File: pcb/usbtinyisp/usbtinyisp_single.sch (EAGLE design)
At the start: 20 parts, among them IC1 ATTINY2313-20P, IC2 74AHC125N

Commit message: update dimensions and change some packages
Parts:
- D1, D2: value 3.6V -> 3V6; device diode:ZENER-DIODEDO35Z10 -> diode:ZENER-DIODESOD80C
- JP1: device pinhead-ez:PINHD-2X3 -> con-ml:ML6
- R1, R2: value 27 -> 68
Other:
- moved on the sheet: C2, D1, D2, LED1, LED2, R1, R2, R3, R5, R6, X1

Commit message: unsmash
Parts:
- C1: value 0.1uF -> 100n
- C2: value 100uF -> 100u
- R10: value 10K -> 10k
- R3, R4, R5, R6, R7: value 1.5K -> 1k5
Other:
- moved on the sheet: C1, IC2P

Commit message: vergessene Änderungen
wenn man nicht alles gleich commited :-/
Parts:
- removed XTL1: 12.0 MHz, minimidi:CERMOSCILL
- added C3, C4: 22p, rcl:C-EUC1206
- added Q1: 12000, crystal:CRYSTALHC49U-V
- IC2: value 74AHC125N -> 74LVX125D; device 74xx-eu:74HC125N -> 74xx-eu:74HC125D
- R1, R10, R4, R7: device rcl-ez:R-US_0207/10 -> rcl:R-EU_R0805
- R2, R3, R5, R6: device rcl-ez:R-US_0207/5V -> rcl:R-EU_R0805
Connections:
- removed net N$4: IC1.XTAL1(PA0), XTL1.OUT
- removed net N$5: IC1.XTAL2(PA1), XTL1.IN
- new net XTAL1: C4.1, IC1.XTAL1(PA0), Q1.1
- new net XTAL2: C3.1, IC1.XTAL2(PA1), Q1.2
- net GND: now also C3.2, C4.2; no longer XTL1.GND
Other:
- moved on the sheet: C1

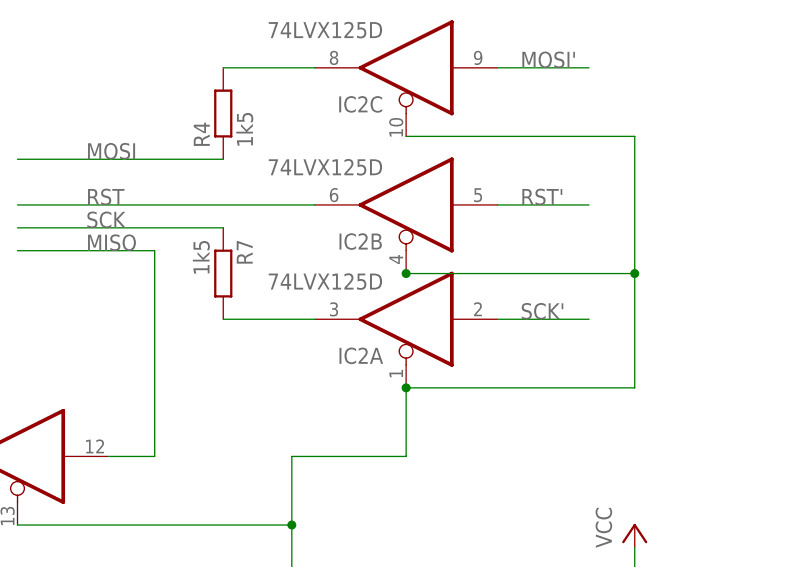
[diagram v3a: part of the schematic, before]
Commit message: swapped some gates and moved all parts around
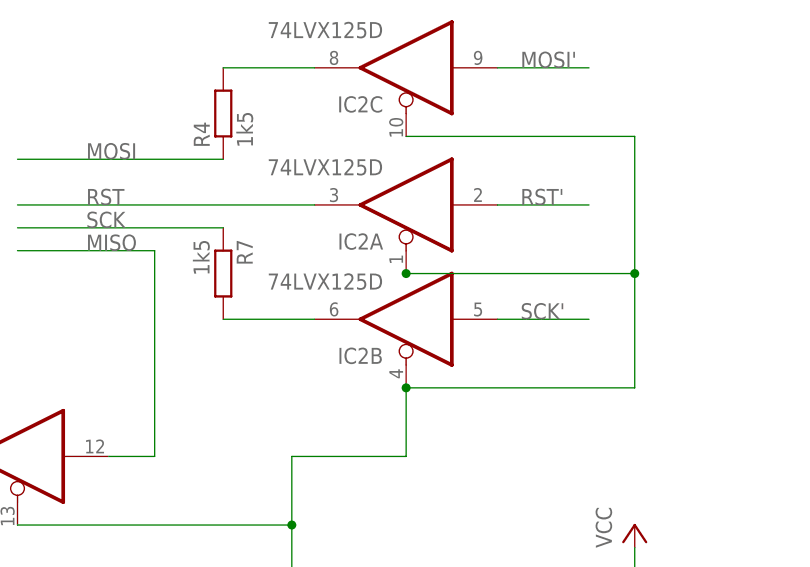
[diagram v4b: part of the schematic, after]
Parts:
- R1, R2: device rcl:R-EU_R0805 -> rcl:R-EU_0207/10
- R7: device rcl:R-EU_R0805 -> rcl:R-EU_0207/12
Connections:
- net N$12: now also IC2B.O; no longer IC2A.O
- net RST: now also IC2A.O; no longer IC2B.O
- net RST': now also IC2A.I; no longer IC2B.I
- net SCK': now also IC2B.I; no longer IC2A.I
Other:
- moved on the sheet: IC2A, IC2B
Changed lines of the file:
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@@
 </classes>
 <parts>
-<part name="R1" library="rcl" deviceset="R-EU_" device="R0805" value="68"/>
-<part name="R2" library="rcl" deviceset="R-EU_" device="R0805" value="68"/>
+<part name="R1" library="rcl" deviceset="R-EU_" device="0207/10" value="68"/>
+<part name="R2" library="rcl" deviceset="R-EU_" device="0207/10" value="68"/>
 <part name="R3" library="rcl" deviceset="R-EU_" device="R0805" value="1k5"/>
 <part name="GND1" library="supply1" deviceset="GND" device=""/>
@@
 <part name="D1" library="diode" deviceset="ZENER-DIODE" device="SOD80C" value="3V6"/>
 <part name="D2" library="diode" deviceset="ZENER-DIODE" device="SOD80C" value="3V6"/>
-<part name="R7" library="rcl" deviceset="R-EU_" device="R0805" value="1k5"/>
+<part name="R7" library="rcl" deviceset="R-EU_" device="0207/12" value="1k5"/>
 <part name="R4" library="rcl" deviceset="R-EU_" device="R0805" value="1k5"/>
 <part name="P+3" library="supply1" deviceset="VCC" device=""/>
@@
 <instance part="JP1" gate="1" x="53.34" y="152.4" rot="MR180"/>
 <instance part="X1" gate="G$1" x="20.32" y="76.2" rot="MR0"/>
-<instance part="IC2" gate="A" x="127" y="142.24" rot="R180"/>
-<instance part="IC2" gate="B" x="127" y="154.94" rot="R180"/>
+<instance part="IC2" gate="B" x="127" y="142.24" rot="R180"/>
+<instance part="IC2" gate="A" x="127" y="154.94" rot="R180"/>
 <instance part="IC2" gate="C" x="127" y="170.18" rot="R180"/>
 <instance part="IC2" gate="D" x="83.82" y="127" rot="R180"/>
@@
 <wire x1="116.84" y1="154.94" x2="83.82" y2="154.94" width="0.1524" layer="91"/>
 <label x="91.44" y="154.94" size="1.778" layer="95"/>
-<pinref part="IC2" gate="B" pin="O"/>
+<pinref part="IC2" gate="A" pin="O"/>
 </segment>
 <segment>
@@
 <wire x1="106.68" y1="142.24" x2="116.84" y2="142.24" width="0.1524" layer="91"/>
 <pinref part="R7" gate="G$1" pin="2"/>
-<pinref part="IC2" gate="A" pin="O"/>
+<pinref part="IC2" gate="B" pin="O"/>
 </segment>
 </net>
@@
 <wire x1="137.16" y1="154.94" x2="147.32" y2="154.94" width="0.1524" layer="91"/>
 <label x="139.7" y="154.94" size="1.778" layer="95"/>
-<pinref part="IC2" gate="B" pin="I"/>
+<pinref part="IC2" gate="A" pin="I"/>
 </segment>
 </net>
@@
 <wire x1="137.16" y1="142.24" x2="147.32" y2="142.24" width="0.1524" layer="91"/>
 <label x="139.7" y="142.24" size="1.778" layer="95"/>
-<pinref part="IC2" gate="A" pin="I"/>
+<pinref part="IC2" gate="B" pin="I"/>
 </segment>
 </net>
@@
 <pinref part="IC1" gate="G$1" pin="(T0)PD4"/>
 <pinref part="IC2" gate="C" pin="OE"/>
+<pinref part="IC2" gate="A" pin="OE"/>
 <pinref part="IC2" gate="B" pin="OE"/>
-<pinref part="IC2" gate="A" pin="OE"/>
 <pinref part="IC2" gate="D" pin="OE"/>
 <junction x="152.4" y="147.32"/>

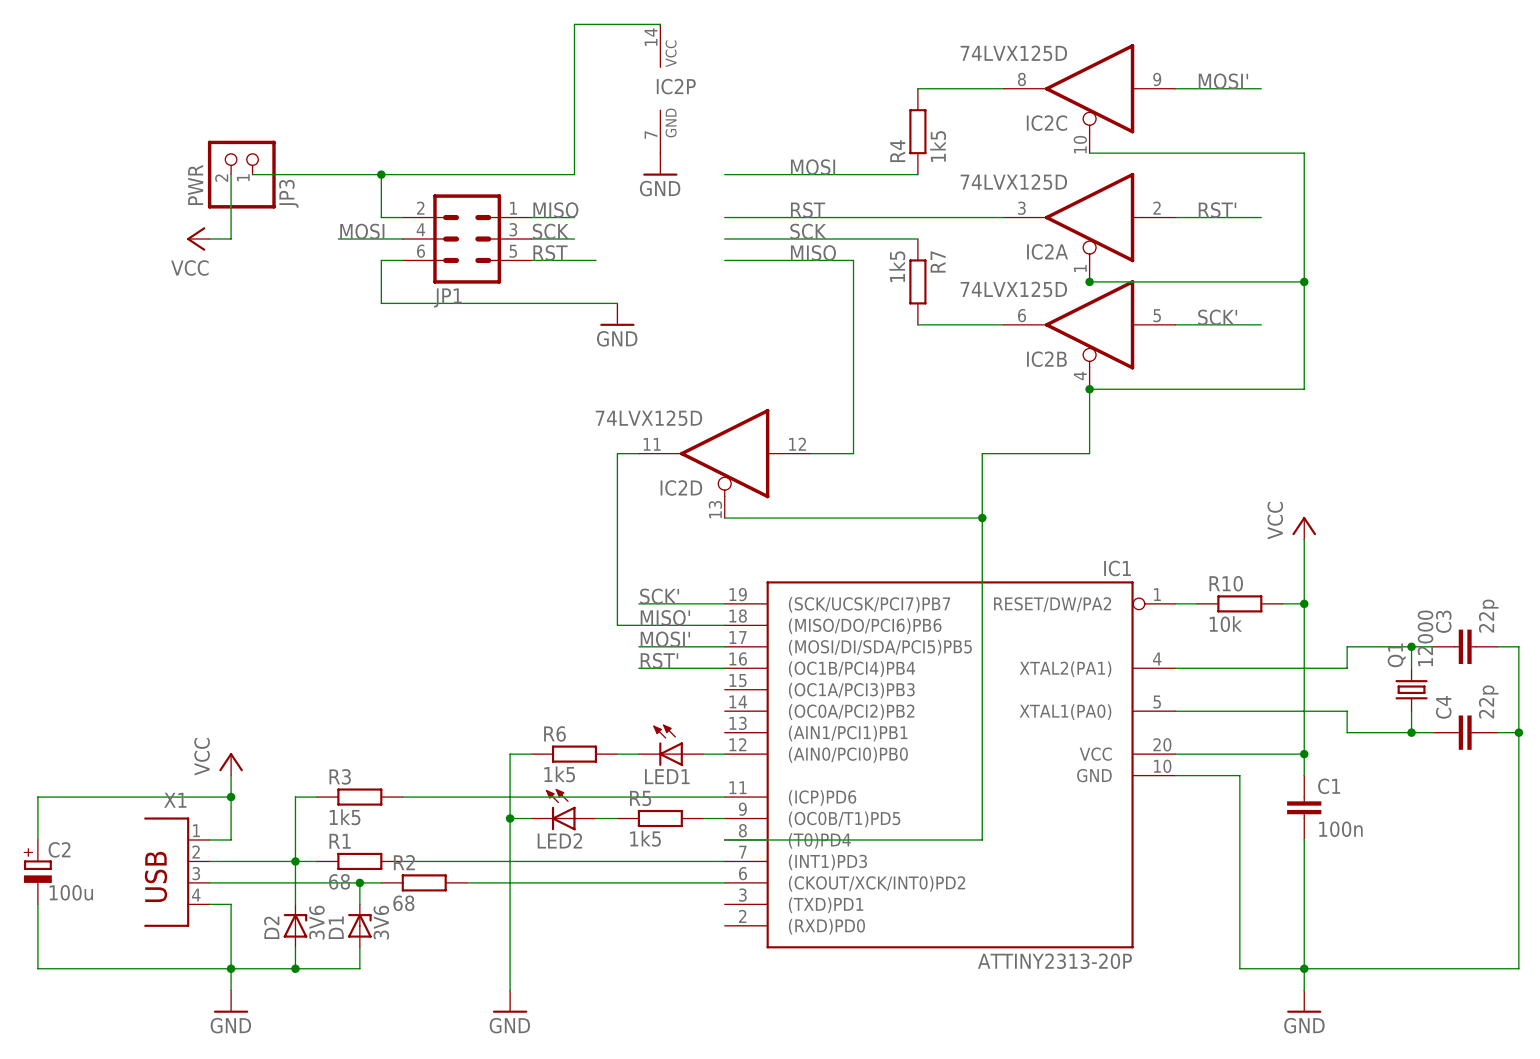
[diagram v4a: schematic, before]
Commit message: routed
ready for soldering (first test)
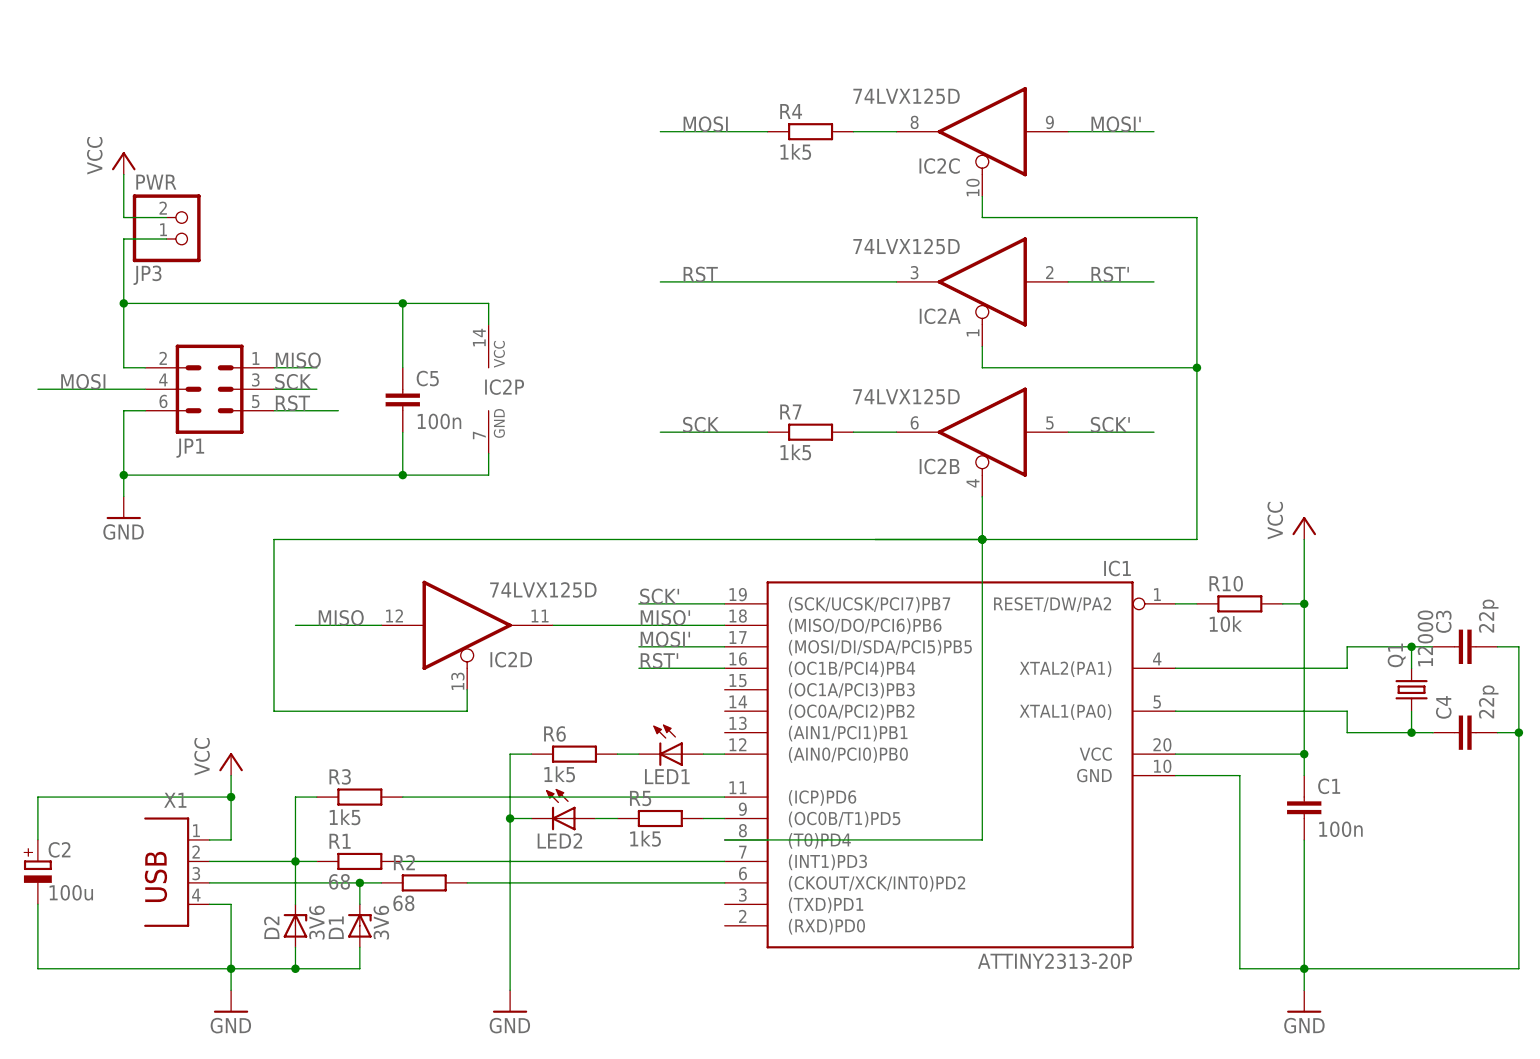
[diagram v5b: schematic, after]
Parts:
- added C5: 100n, rcl:C-EUC0805
- R7: device rcl:R-EU_0207/12 -> rcl:R-EU_0207/10
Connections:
- removed net N$14: IC2P.VCC, JP1.2, JP3.1
- new net VTARGET: C5.1, IC2P.VCC, JP1.2, JP3.1
- net GND: now also C5.2
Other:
- moved on the sheet: IC2A, IC2B, IC2C, IC2D, IC2P, JP1, JP3, R4, R7
